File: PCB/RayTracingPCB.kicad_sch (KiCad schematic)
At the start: 1 part, among them J1 Conn_ARM_JTAG_SWD_10

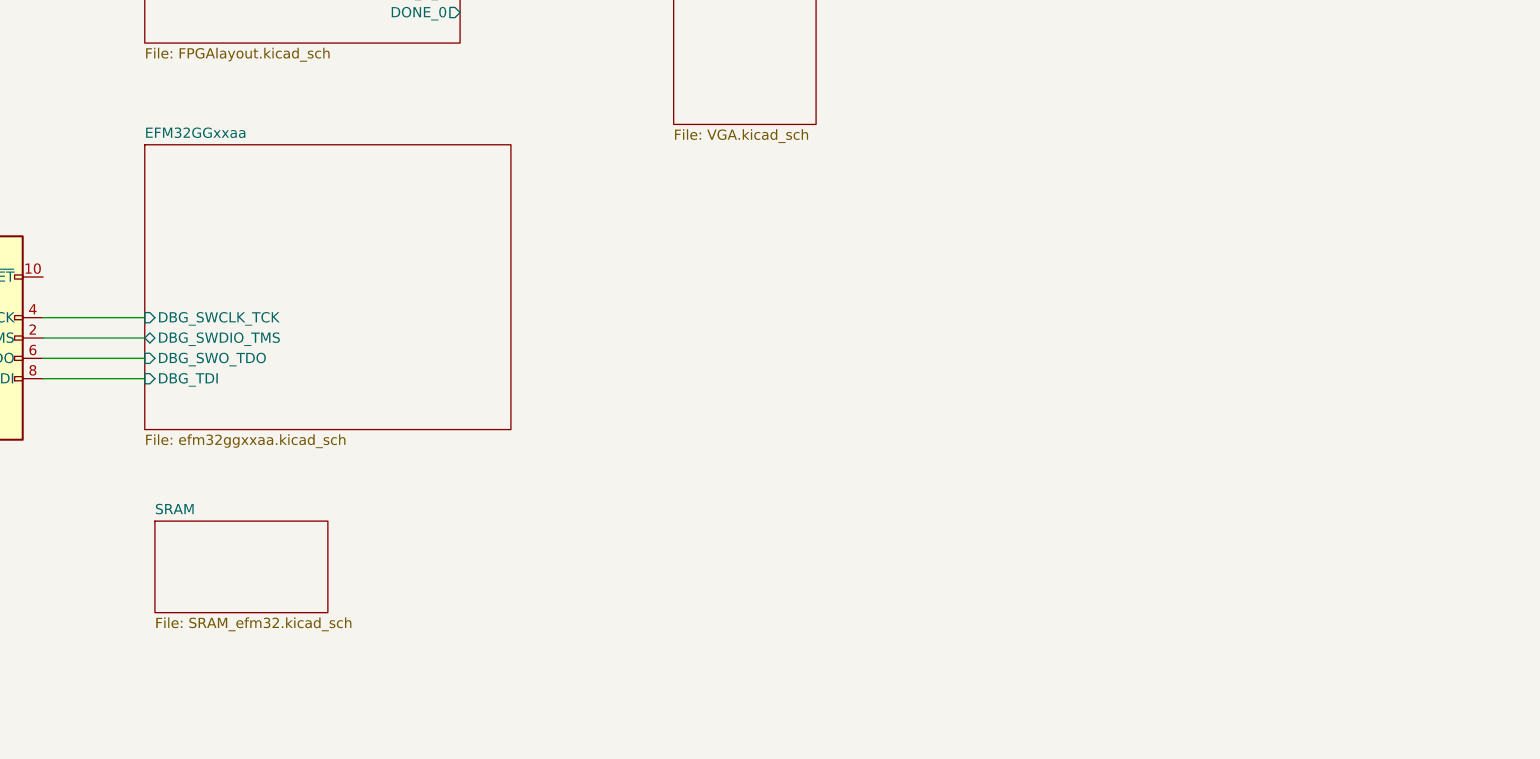
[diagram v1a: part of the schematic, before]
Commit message: Trace MCU Master to SRAM Slave
Signed-off-by: Daniel Yang Hansen <daniel.yang.hansen@gmail.com>
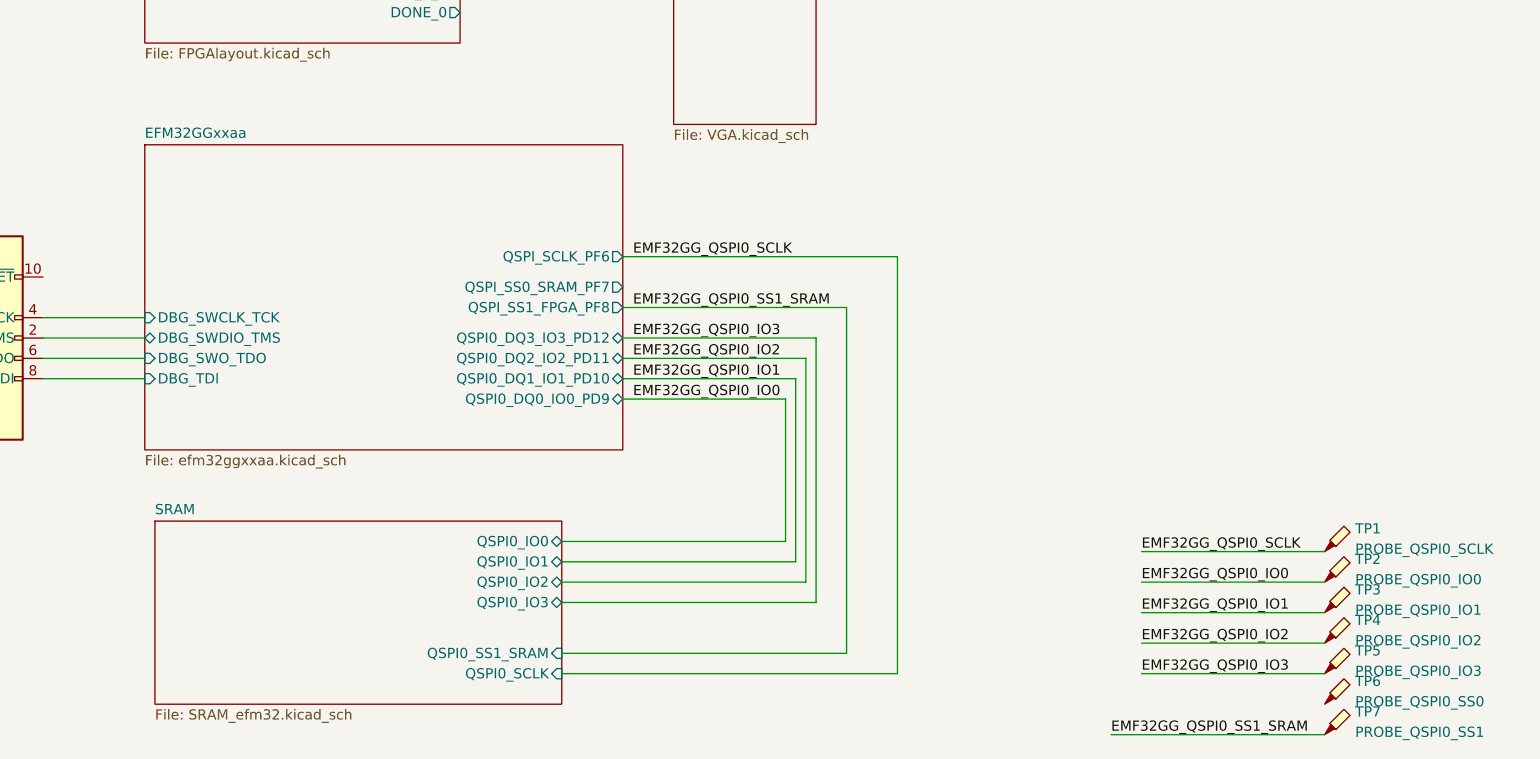
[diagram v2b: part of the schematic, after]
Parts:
- added TP1: PROBE_QSPI0_SCLK, symbol Connector:TestPoint_Probe
- added TP2: PROBE_QSPI0_IO0, symbol Connector:TestPoint_Probe
- added TP3: PROBE_QSPI0_IO1, symbol Connector:TestPoint_Probe
- added TP4: PROBE_QSPI0_IO2, symbol Connector:TestPoint_Probe
- added TP5: PROBE_QSPI0_IO3, symbol Connector:TestPoint_Probe
- added TP6: PROBE_QSPI0_SS0, symbol Connector:TestPoint_Probe
- added TP7: PROBE_QSPI0_SS1, symbol Connector:TestPoint_Probe
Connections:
- new net EMF32GG_QSPI0_IO0: TP2.1
- new net EMF32GG_QSPI0_IO1: TP3.1
- new net EMF32GG_QSPI0_IO2: TP4.1
- new net EMF32GG_QSPI0_IO3: TP5.1
- new net EMF32GG_QSPI0_SCLK: TP1.1
- new net EMF32GG_QSPI0_SS1_SRAM: TP7.1
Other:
- sheet EFM32GGxxaa ports: added QSPI0_DQ0_IO0_PD9, QSPI0_DQ1_IO1_PD10, QSPI0_DQ2_IO2_PD11, QSPI0_DQ3_IO3_PD12, QSPI_SCLK_PF6, QSPI_SS0_SRAM_PF7, QSPI_SS1_FPGA_PF8; removed none
- sheet SRAM ports: added QSPI0_IO0, QSPI0_IO1, QSPI0_IO2, QSPI0_IO3, QSPI0_SCLK, QSPI0_SS1_SRAM; removed none

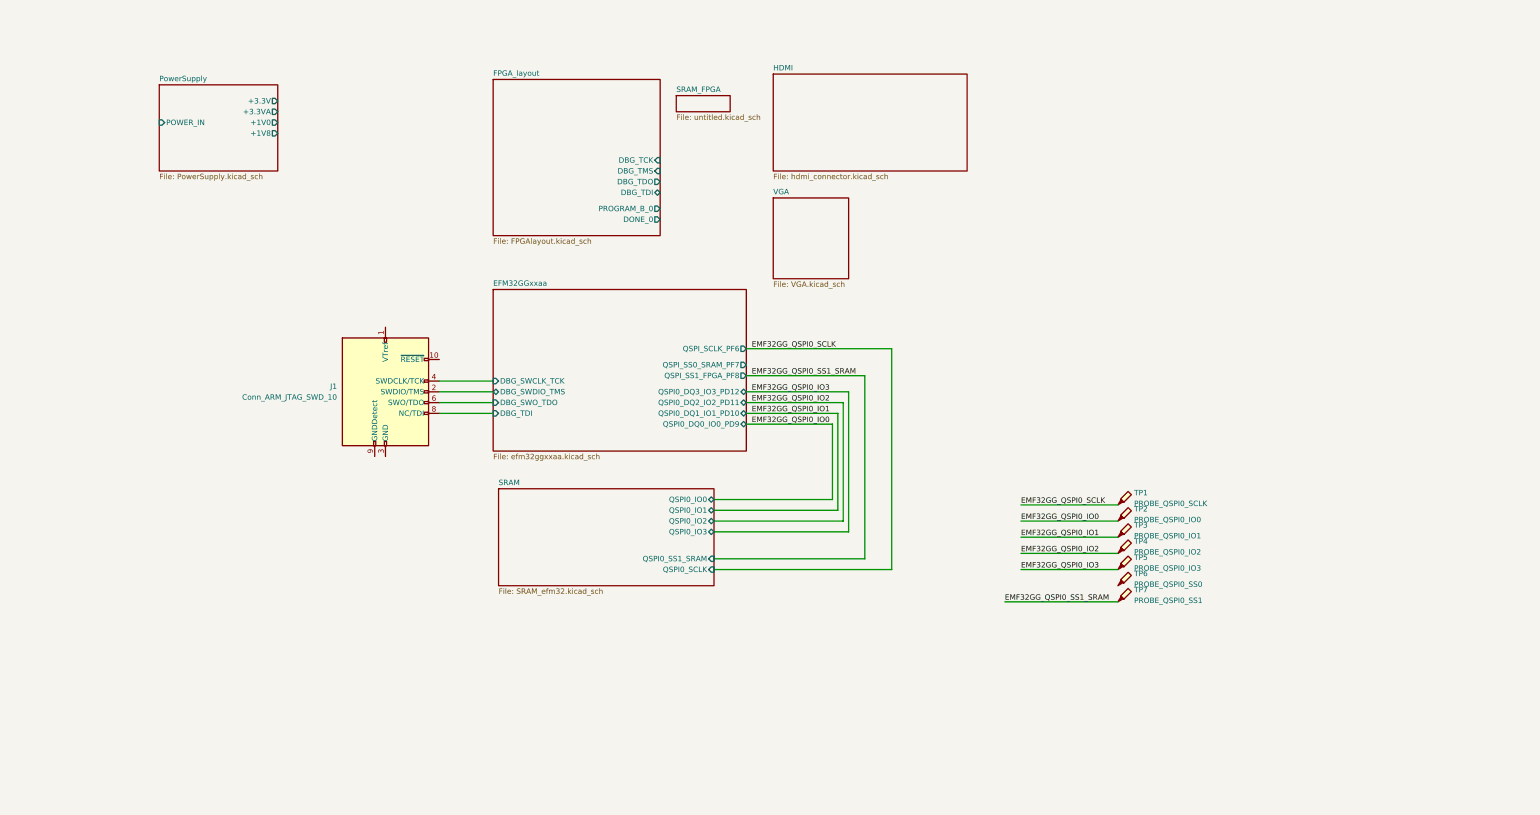
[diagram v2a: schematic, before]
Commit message: Finish MCU Master to Slave Traces for QSPI and Reorganize RootSheet
Signed-off-by: Daniel Yang Hansen <daniel.yang.hansen@gmail.com>
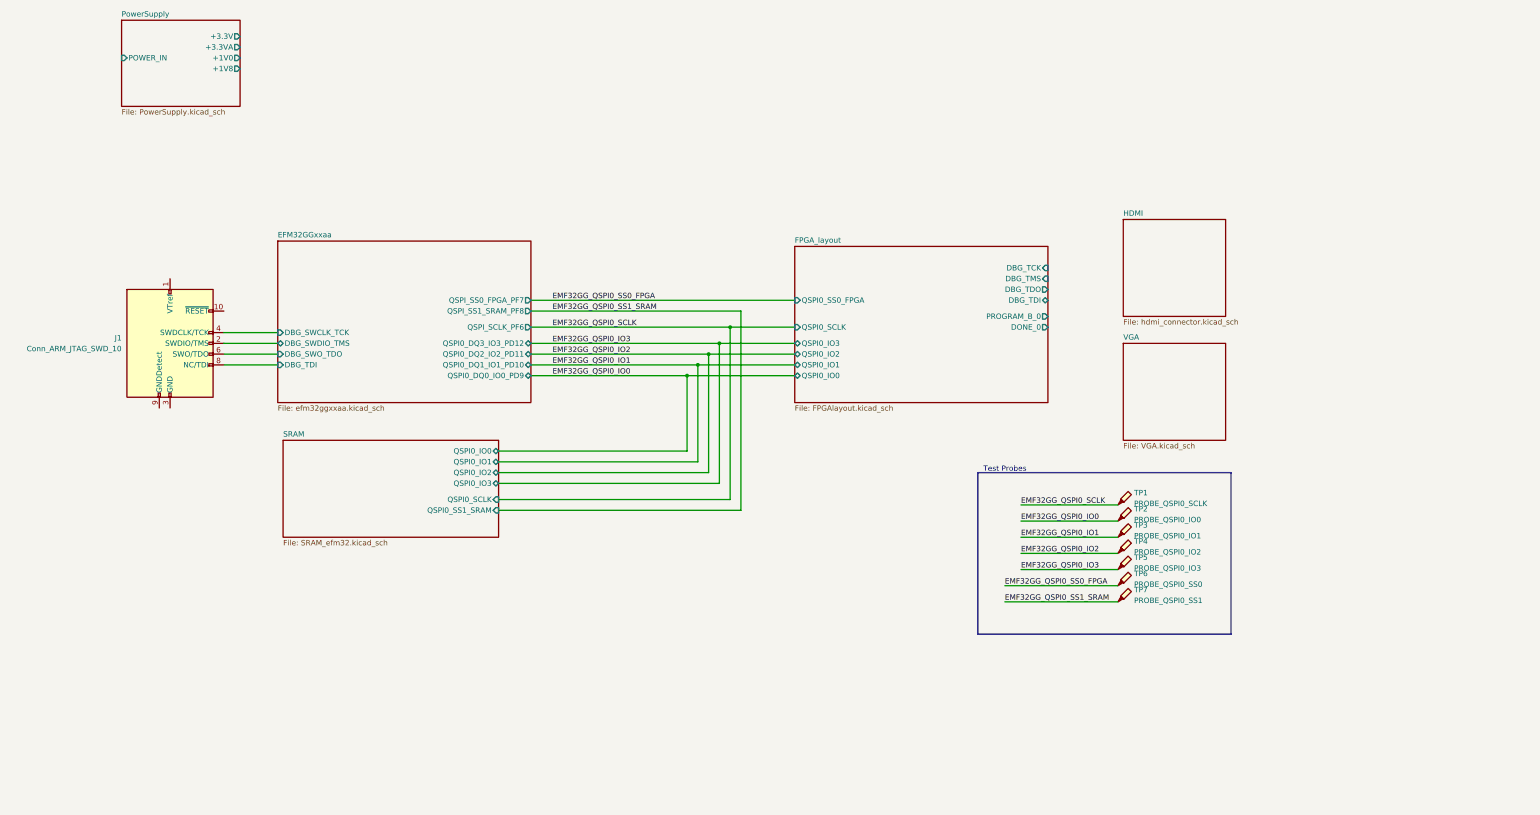
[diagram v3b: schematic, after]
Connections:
- net EMF32GG_QSPI0_SS0_FPGA: now reaches TP6.1
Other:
- removed sheet SRAM_FPGA
- sheet EFM32GGxxaa ports: added QSPI_SS0_FPGA_PF7, QSPI_SS1_SRAM_PF8; removed QSPI_SS0_SRAM_PF7, QSPI_SS1_FPGA_PF8
- sheet FPGA_layout ports: added QSPI0_IO0, QSPI0_IO1, QSPI0_IO2, QSPI0_IO3, QSPI0_SCLK, QSPI0_SS0_FPGA; removed none
- note added: "Test Probes"
- moved on the sheet: J1

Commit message: dump
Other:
- sheet PowerSupply ports: added none; removed +1V0, +1V8, +3.3V, +3.3VA
- sheet VGA ports: added VGA_B0, VGA_B1, VGA_B2, VGA_B3, VGA_G0, VGA_G1, VGA_G2, VGA_G3, VGA_HSync, VGA_R0, VGA_R1, VGA_R2, VGA_R3, VGA_VSync; removed none
- moved on the sheet: J1, TP1, TP2, TP3, TP4, TP5, TP6, TP7

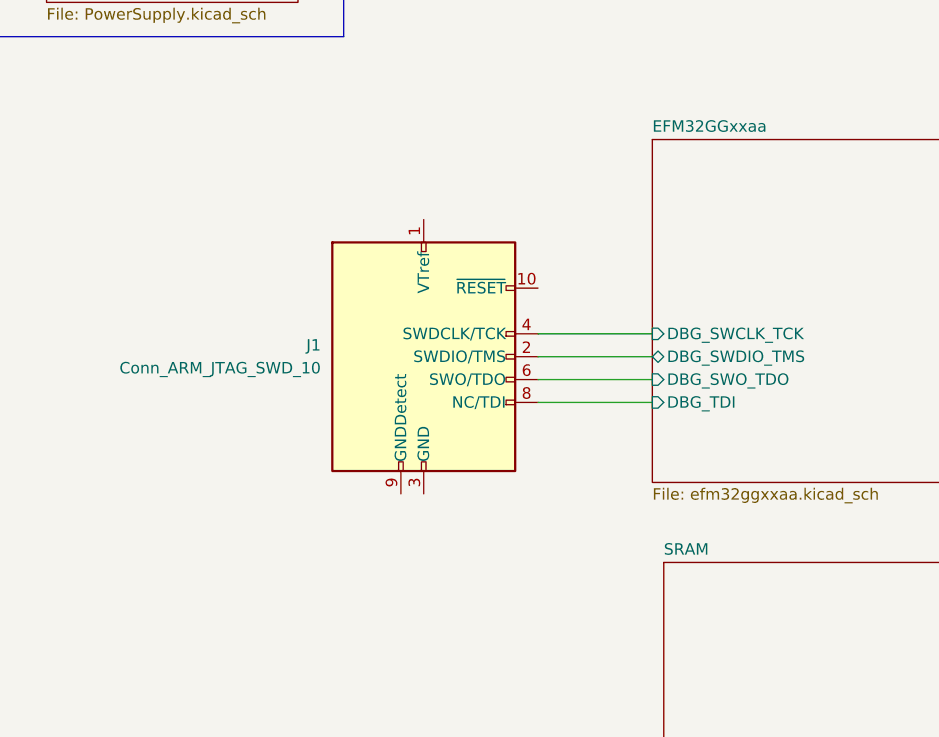
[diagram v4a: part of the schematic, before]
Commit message: Clean up MCU ++
Signed-off-by: Daniel Yang Hansen <daniel.yang.hansen@gmail.com>
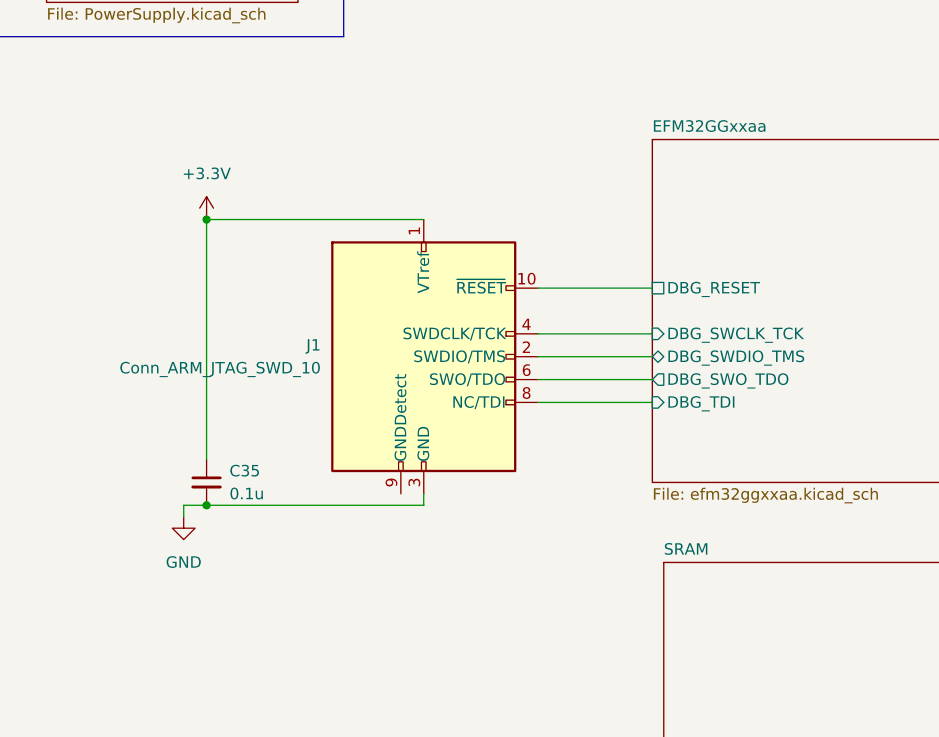
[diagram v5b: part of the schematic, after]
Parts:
- added C35: 0.1u, symbol Device:C_Small
- J1: Info / Help (none) -> https://developer.arm.com/documentation/101416/0100/Hardwar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
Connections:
- net +3.3V: now reaches J1.1 (VTref)
- net +3.3V: now also C35.1
- net EFM32GGxxaa/DBG_RESET: now reaches J1.10 (~{RESET})
- net GND: now reaches J1.3 (GND), J1.5 (GND)
- net GND: now also C35.2
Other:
- sheet EFM32GGxxaa ports: added DBG_RESET; removed none
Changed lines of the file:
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@@
   (junction (at 220.98 90.17) (diameter 0) (color 162 255 50 1)
   )
+  (junction (at 64.77 110.49) (diameter 0) (color 0 0 0 0)
+  )
   (junction (at 218.44 93.98) (diameter 0) (color 0 0 0 0)
+  )
+  (junction (at 64.77 78.74) (diameter 0) (color 0 0 0 0)
   )
   (junction (at 215.9 96.52) (diameter 0) (color 0 0 0 0)
@@
     (stroke (width 0) (type default) (color 162 255 50 1))
   )
+  (wire (pts (xy 64.77 78.74) (xy 64.77 105.41))
+    (stroke (width 0) (type default))
+  )
   (wire (pts (xy 218.44 93.98) (xy 218.44 127))
+    (stroke (width 0) (type default))
+  )
+  (wire (pts (xy 88.9 110.49) (xy 88.9 109.22))
     (stroke (width 0) (type default))
   )
@@
     (stroke (width 0) (type default))
   )
+  (wire (pts (xy 64.77 110.49) (xy 88.9 110.49))
+    (stroke (width 0) (type default))
+  )
+  (wire (pts (xy 64.77 78.74) (xy 88.9 78.74))
+    (stroke (width 0) (type default))
+  )
   (wire (pts (xy 173.99 96.52) (xy 215.9 96.52))
     (stroke (width 0) (type default))
@@
     (stroke (width 0) (type default))
   )
+  (wire (pts (xy 62.23 110.49) (xy 64.77 110.49))
+    (stroke (width 0) (type default))
+  )
   (wire (pts (xy 210.82 101.6) (xy 236.22 101.6))
     (stroke (width 0) (type default))
@@
     (stroke (width 0) (type default))
   )
+  (wire (pts (xy 114.3 86.36) (xy 101.6 86.36))
+    (stroke (width 0) (type default))
+  )
   (wire (pts (xy 218.44 93.98) (xy 236.22 93.98))
     (stroke (width 0) (type default))
@@
   (wire (pts (xy 220.98 90.17) (xy 220.98 130.81))
     (stroke (width 0) (type default) (color 162 255 50 1))
+  )
+  (wire (pts (xy 62.23 110.49) (xy 62.23 111.76))
+    (stroke (width 0) (type default))
   )
   (wire (pts (xy 101.6 99.06) (xy 114.3 99.06))
@@
     (effects (font (size 1.27 1.27)) (justify left bottom))
   )
+  (symbol (lib_id "power:GND") (at 62.23 111.76 0) (unit 1)
+    (in_bom yes) (on_board yes) (dnp no) (fields_autoplaced)
+    (property "Reference" "#PWR013" (at 62.23 118.11 0)
+      (effects (font (size 1.27 1.27)) hide)
+    )
+    (property "Value" "GND" (at 62.23 116.84 0)
+      (effects (font (size 1.27 1.27)))
+    )
+    (property "Footprint" "" (at 62.23 111.76 0)
+      (effects (font (size 1.27 1.27)) hide)
+    )
+    (property "Datasheet" "" (at 62.23 111.76 0)
+      (effects (font (size 1.27 1.27)) hide)
+    )
+    (pin "1")
+    (instances
+      (project "RayTracingPCB"
+        (path "/e9047d94-28be-4266-894b-6ee25ef088bd"
+          (reference "#PWR013") (unit 1)
+        )
+      )
+    )
+  )
   (symbol (lib_id "Connector:TestPoint_Probe") (at 68.58 185.42 0) (unit 1)
     (in_bom yes) (on_board yes) (dnp no) (fields_autoplaced)
@@
     )
   )
+  (symbol (lib_id "Device:C_Small") (at 64.77 107.95 0) (unit 1)
+    (in_bom yes) (on_board yes) (dnp no) (fields_autoplaced)
+    (property "Reference" "C35" (at 67.31 106.6863 0)
+      (effects (font (size 1.27 1.27)) (justify left))
+    )
+    (property "Value" "0.1u" (at 67.31 109.2263 0)
+      (effects (font (size 1.27 1.27)) (justify left))
+    )
+    (property "Footprint" "" (at 64.77 107.95 0)
+      (effects (font (size 1.27 1.27)) hide)
+    )
+    (property "Datasheet" "~" (at 64.77 107.95 0)
+      (effects (font (size 1.27 1.27)) hide)
+    )
+    (pin "1")
+    (pin "2")
+    (instances
+      (project "RayTracingPCB"
+        (path "/e9047d94-28be-4266-894b-6ee25ef088bd/5a7a2c0a-f09d-4b4f-9411-f51dd121457c"
+          (reference "C35") (unit 1)
+        )
+        (path "/e9047d94-28be-4266-894b-6ee25ef088bd/f9a74965-bde5-47a2-9f66-243cb6fc0f53"
+          (reference "C24") (unit 1)
+        )
+        (path "/e9047d94-28be-4266-894b-6ee25ef088bd"
+          (reference "C25") (unit 1)
+        )
+      )
+    )
+  )
   (symbol (lib_id "Connector:TestPoint_Probe") (at 68.58 196.85 0) (unit 1)
     (in_bom yes) (on_board yes) (dnp no) (fields_autoplaced)
@@
     )
     (property "Datasheet" "http://infocenter.arm.com/help/topic/com.arm.doc.ddi0314h/DDI0314H_coresight_components_trm.pdf" (at 80.01 125.73 90)
+      (effects (font (size 1.27 1.27)) hide)
+    )
+    (property "Info / Help" "https://developer.arm.com/documentation/101416/0100/Hardware-Description/Target-Interfaces/Cortex-Debug--10-pin-" (at 88.9 93.98 0)
       (effects (font (size 1.27 1.27)) hide)
     )
@@
     )
   )
+  (symbol (lib_id "power:+3.3V") (at 64.77 78.74 0) (unit 1)
+    (in_bom yes) (on_board yes) (dnp no) (fields_autoplaced)
+    (property "Reference" "#PWR017" (at 64.77 82.55 0)
+      (effects (font (size 1.27 1.27)) hide)
+    )
+    (property "Value" "+3.3V" (at 64.77 73.66 0)
+      (effects (font (size 1.27 1.27)))
+    )
+    (property "Footprint" "" (at 64.77 78.74 0)
+      (effects (font (size 1.27 1.27)) hide)
+    )
+    (property "Datasheet" "" (at 64.77 78.74 0)
+      (effects (font (size 1.27 1.27)) hide)
+    )
+    (pin "1")
+    (instances
+      (project "RayTracingPCB"
+        (path "/e9047d94-28be-4266-894b-6ee25ef088bd"
+          (reference "#PWR017") (unit 1)
+        )
+      )
+    )
+  )
   (symbol (lib_id "Connector:TestPoint_Probe") (at 68.58 193.04 0) (unit 1)
     (in_bom yes) (on_board yes) (dnp no) (fields_autoplaced)
@@
       (effects (font (size 1.27 1.27)) (justify left))
     )
-    (pin "DBG_SWO_TDO" input (at 114.3 96.52 180)
+    (pin "DBG_SWO_TDO" output (at 114.3 96.52 180)
       (effects (font (size 1.27 1.27)) (justify left))
     )
@@
       (effects (font (size 1.27 1.27)) (justify right))
     )
-    (instances
+    (pin "DBG_RESET" passive (at 114.3 86.36 180)
+      (effects (font (size 1.27 1.27)) (justify left))
+    )
+    (instances
